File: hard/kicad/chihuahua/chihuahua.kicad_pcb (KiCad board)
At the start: 2 copper layers, 97.8 x 72.4 mm, 36 parts, among them J1 CARTRIDGE, J2 VIAport, J3 IOx, J4 nanoLink, J5 STEP, J6 POWER, Q1 BC548, Q2 BC548, SW1 RESET, SW2 NMI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

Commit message: mostly routed Chihuahua
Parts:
- JP4: value CA1L -> LATCH; footprint Connector_PinHeader_2.54mm:PinHeader_1x02_P2.54mm_Horizontal -> Connector_PinHeader_2.54mm:PinHeader_1x02_P2.54mm_Vertical
- R3, R4: value R -> 3K3
- R5: value R -> 1K
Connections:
- net /VIA_~IRQ renamed /~VREQ
- net Net-(JP3-Pad1) renamed /~VP
- SW1 pad 1: +5V -> /U_RST
- SW1 pad 2: /U_RST -> +5V
- U4 pad 10: /VIA_~CS -> /~IOC
- U4 pad 11: /ROM_~CS -> /ROM_~OE
- U4 pad 12: A15 -> /R~W
- U4 pad 13: /~IOC -> /VIA_~CS
- U4 pad 8: /ROM_~OE -> /ROM_~CS
- U4 pad 9: /R~W -> A15
- U5 pad 1: /R~W -> /CB2
- U5 pad 10: /CB2 -> PB7
- U5 pad 11: /CB2 -> /~WE
- U5 pad 12: /CB2 -> /R~W
- U5 pad 13: /CB2 -> /PHI1
- U5 pad 2: /PHI1 -> /CB2
- U5 pad 3: /~WE -> /CB2
- U5 pad 4: PB7 -> /CB2
- U5 pad 5: PB7 -> /CB2
- U5 pad 6: PB7 -> /CB2
- U5 pad 8: /CB2 -> PB7
- U5 pad 9: /CB2 -> PB7
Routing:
- net /~NMI: track 21.8 -> 127.0 mm, vias 0 -> 3
- net /~WE: track 91.4 -> 0.00 mm, vias 2 -> 0
- net +5V: track 230.8 -> 300.6 mm, vias 1 -> 4
- net /~IOC: track 0.00 -> 66.0 mm, vias 0 -> 1
- net GND: track 340.9 -> 279.3 mm
- net /CA2: track 52.4 -> 0.00 mm, vias 1 -> 0
- net /CA1: track 46.6 -> 0.00 mm, vias 1 -> 0
- net A10: track 26.6 -> 69.0 mm, vias 0 -> 1
- net A11: track 26.6 -> 66.6 mm, vias 0 -> 1
- net PB2: track 4.86 -> 40.4 mm, vias 0 -> 1
- net PB1: track 4.86 -> 39.5 mm, vias 0 -> 1
- net PB0: track 4.86 -> 38.6 mm, vias 0 -> 1
- net A9: track 26.6 -> 59.5 mm, vias 0 -> 1
- net A0: track 42.8 -> 71.3 mm, vias 0 -> 1
- net A1: track 42.8 -> 70.9 mm, vias 0 -> 1
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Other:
- net class Default: clearance 0.2 -> 0.15; trace_width 0.25 -> 0.2; via_dia 0.8 -> 0.55; via_drill 0.4 -> 0.35
- net class LowZ added: clearance 0.2, trace_width 0.635, via_dia 0.8, via_drill 0.5
- net class Power added: clearance 0.15, trace_width 0.28, via_dia 0.55, via_drill 0.35
- rule trace_clearance: 0.2 -> 0.15
- rule trace_min: 0.2 -> 0.127
- rule via_min_size: 0.4 -> 0.5

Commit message: completely routed Chihuahua
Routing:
- net /CA1: track 0.00 -> 162.0 mm, vias 0 -> 3
- net /ROM_~CS: track 0.00 -> 93.4 mm, vias 0 -> 3
- net /ROM_~OE: track 0.00 -> 84.3 mm, vias 0 -> 2
- net /~WE: track 0.00 -> 75.9 mm
- net /VIA_CS: track 0.00 -> 67.4 mm, vias 0 -> 2
- net /CA2: track 0.00 -> 66.9 mm, vias 0 -> 3
- net /PHI1: track 0.00 -> 61.8 mm, vias 0 -> 1
- net +5V: track 300.6 -> 360.6 mm, vias 4 -> 5
- net /VIA_~CS: track 0.00 -> 35.3 mm, vias 0 -> 3
- net /CB2: track 69.8 -> 104.9 mm, vias 1 -> 2
- net PB4: track 42.2 -> 74.2 mm, vias 1 -> 2
- net PB3: track 41.3 -> 72.9 mm, vias 1 -> 2
- net PB1: track 39.5 -> 70.1 mm, vias 1 -> 3
- net PB0: track 38.6 -> 68.8 mm, vias 1 -> 3
- net PB2: track 40.4 -> 69.8 mm, vias 1 -> 3
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
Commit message: finish silkscreen, not sure about /IOC
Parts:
- added LOGO1: Logo_Open_Hardware_Large, Symbol:OSHW-Symbol_8.9x8mm_SilkScreen, B.Cu at (48.3, 50.8)
- added LOGO2: Logo_Open_Hardware_Small, durango:jaqueria, B.Cu at (91.4, 20.3)
- D1: footprint Diode_THT:D_DO-35_SOD27_P2.54mm_Vertical_AnodeUp -> Diode_THT:D_DO-35_SOD27_P2.54mm_Vertical_KathodeUp
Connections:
- J1 pad 4: /~IOC -> PB5
- U4 pad 10: /~IOC -> PB5
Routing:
- net PB5: track 21.5 -> 114.3 mm, vias 0 -> 2
- net /~IOC: track 66.0 -> 0.00 mm, vias 1 -> 0
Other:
- board text added: "+"
- board text added: "+5 GND PA0 PA5 PA1 PA6 PA2 PA7 PA3 CA1 PA4 CA2 GND +5V"
- board text added: "+5 GND PB0 PB5 PB1 PB6 PB2 PB7 PB3 CB1 PB4 CB2 GND +5V"
- board text added: "+5 PD0 BA0 PD1 BA1 PD2 BA2 PD3 BA3 PD4 /WR PD5 /IO PD6 GND PD7"
- board text added: "@zuiko21"
- board text added: "Chihuahua PLUS v1 (2023·10)"
- board text added: "D"
- board text added: "GND SSCL SSDA ~STB +5"
- board text added: "JLCJLCJLCJLC"
- board text added: "K"
- board text added: "x"
- board text added: "x D C G"
- board text added: "~C"

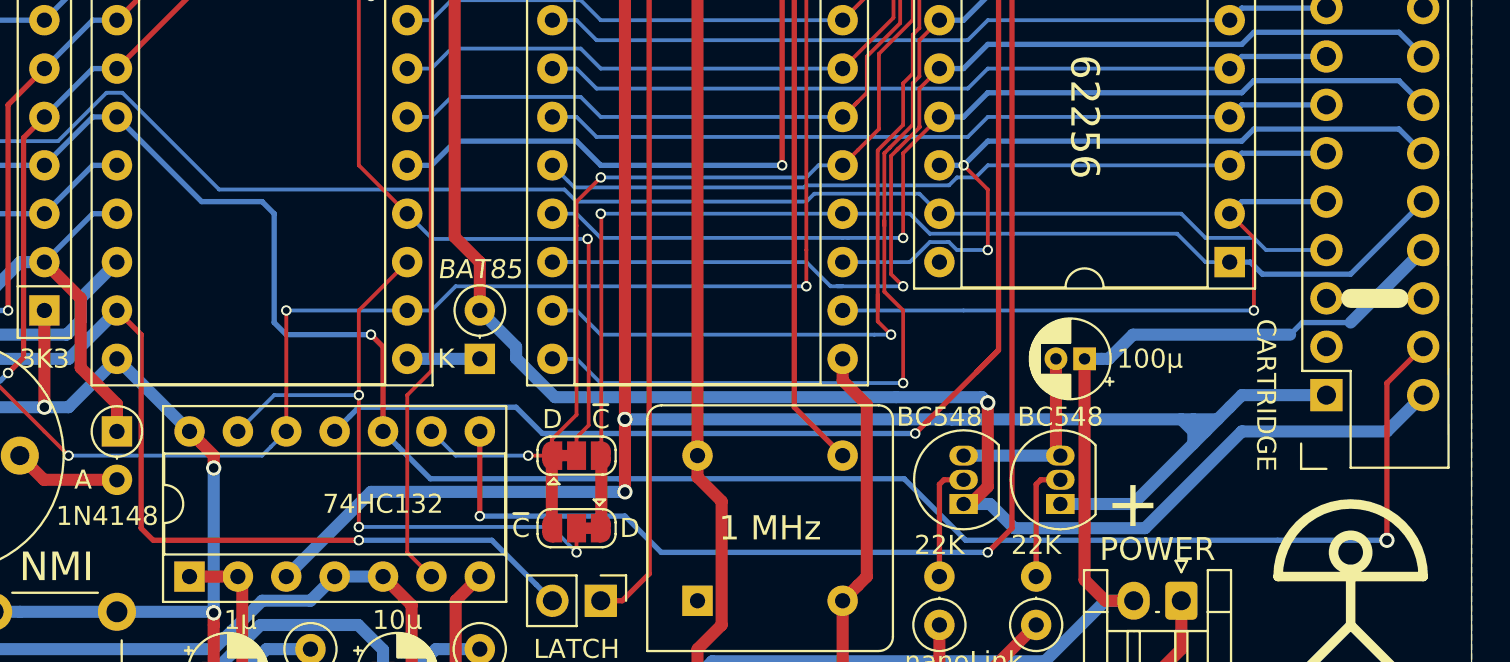
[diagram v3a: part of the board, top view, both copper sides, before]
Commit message: completely remove /IOC from Chihuahua
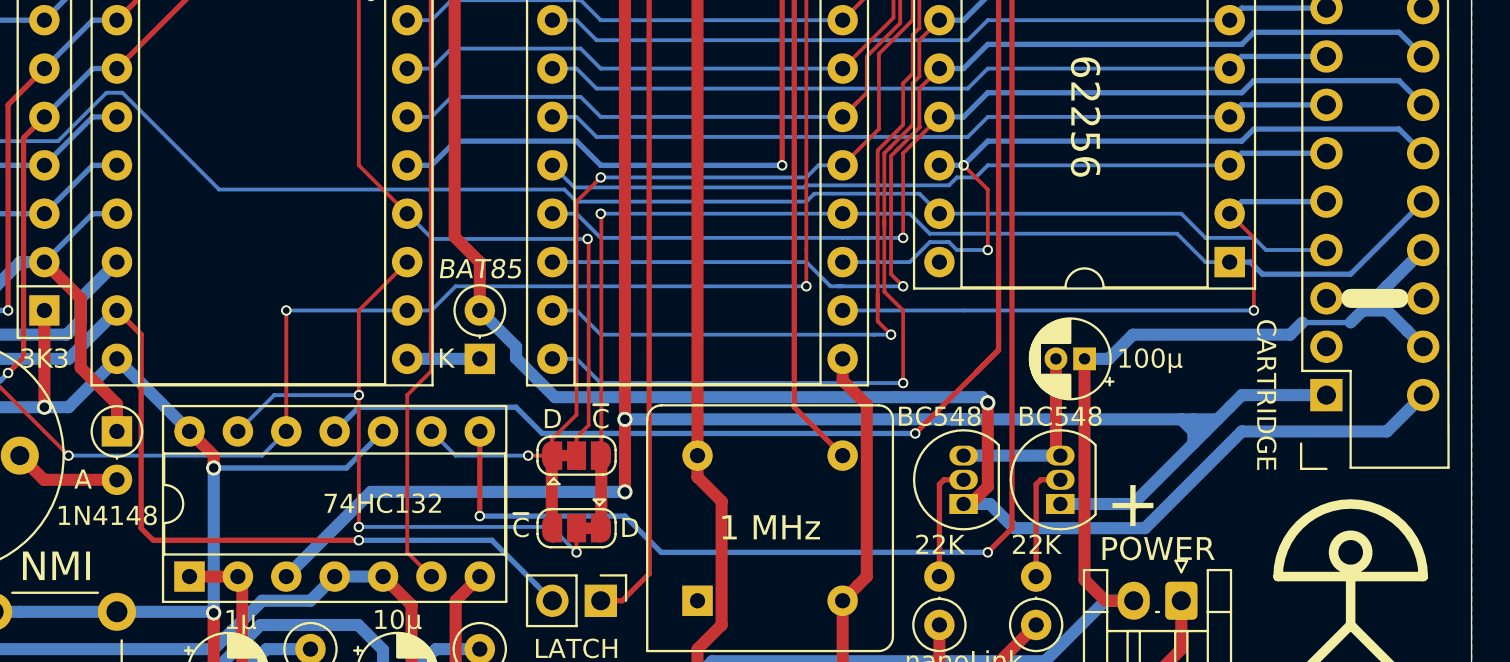
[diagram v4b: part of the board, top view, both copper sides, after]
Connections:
- J1 pad 4: PB5 -> +5V
- U4 pad 10: PB5 -> +5V
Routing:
- net PB5: track 114.3 -> 21.5 mm, vias 2 -> 0
- net +5V: track 360.6 -> 376.4 mm
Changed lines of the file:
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@@
     (thickness 1.6)
     (drawings 31)
-    (tracks 1024)
+    (tracks 1014)
     (zones 0)
     (modules 38)
@@
   )
   (setup
-    (last_trace_width 0.28)
+    (last_trace_width 0.635)
     (user_trace_width 0.2)
     (user_trace_width 0.28)
@@
       (net 68 /U_RST))
     (pad 10 thru_hole oval (at 7.62 10.16 90) (size 1.6 1.6) (drill 0.8) (layers *.Cu *.Mask)
-      (net 17 PB5))
+      (net 2 +5V))
     (pad 3 thru_hole oval (at 0 5.08 90) (size 1.6 1.6) (drill 0.8) (layers *.Cu *.Mask)
       (net 9 /~NMI))
@@
       (net 10 /~IRQ))
     (pad 4 thru_hole oval (at -1.27 5.715 180) (size 1.7 1.7) (drill 1) (layers *.Cu *.Mask)
-      (net 17 PB5))
+      (net 2 +5V))
     (pad 5 thru_hole oval (at 3.81 8.255 180) (size 1.7 1.7) (drill 1) (layers *.Cu *.Mask))
     (pad 3 thru_hole oval (at 3.81 5.715 180) (size 1.7 1.7) (drill 1) (layers *.Cu *.Mask))
@@
   (segment (start 19.111101 18.988899) (end 26.380299 18.988899) (width 0.635) (layer B.Cu) (net 2))
   (segment (start 17.78 20.32) (end 19.111101 18.988899) (width 0.635) (layer B.Cu) (net 2))
-  (segment (start 105.41 64.135) (end 109.22 60.325) (width 0.635) (layer B.Cu) (net 2))
-  (segment (start 91.44 66.04) (end 92.32 66.04) (width 0.635) (layer B.Cu) (net 2))
   (segment (start 92.535 78.74) (end 94.02 78.74) (width 0.635) (layer F.Cu) (net 2))
   (segment (start 91.44 77.645) (end 92.535 78.74) (width 0.635) (layer F.Cu) (net 2))
@@
   (segment (start 71.12 27.94) (end 78.74 27.94) (width 0.635) (layer B.Cu) (net 2))
   (segment (start 68.58 27.94) (end 71.12 27.94) (width 0.635) (layer B.Cu) (net 2))
-  (segment (start 92.32 66.04) (end 92.71 66.04) (width 0.635) (layer B.Cu) (net 2))
-  (segment (start 92.71 66.04) (end 93.98 64.77) (width 0.635) (layer B.Cu) (net 2))
-  (segment (start 93.98 64.77) (end 102.235 64.77) (width 0.635) (layer B.Cu) (net 2))
-  (segment (start 102.235 64.77) (end 102.87 64.135) (width 0.28) (layer B.Cu) (net 2))
   (segment (start 102.87 64.135) (end 105.41 64.135) (width 0.28) (layer B.Cu) (net 2))
   (segment (start 17.78 50.8) (end 19.05 49.53) (width 0.28) (layer B.Cu) (net 2))
@@
   (segment (start 32.496799 55.700001) (end 22.404999 55.700001) (width 0.28) (layer B.Cu) (net 17))
   (segment (start 22.225 55.88) (end 21.59 55.88) (width 0.28) (layer B.Cu) (net 17))
+  (segment (start 52.69 71.77) (end 54.61 69.85) (width 0.28) (layer B.Cu) (net 2))
+  (segment (start 45.72 71.77) (end 52.69 71.77) (width 0.28) (layer B.Cu) (net 2))
+  (segment (start 108.370001 64.555001) (end 109.22 65.405) (width 0.635) (layer B.Cu) (net 2))
+  (segment (start 107.315 63.5) (end 107.315 62.23) (width 0.635) (layer B.Cu) (net 2))
+  (segment (start 106.68 62.865) (end 107.315 62.23) (width 0.635) (layer B.Cu) (net 2))
+  (segment (start 107.315 62.23) (end 109.22 60.325) (width 0.635) (layer B.Cu) (net 2))
+  (segment (start 106.68 62.865) (end 107.315 63.5) (width 0.635) (layer B.Cu) (net 2))
+  (segment (start 107.315 63.5) (end 108.370001 64.555001) (width 0.635) (layer B.Cu) (net 2))
+  (segment (start 106.045 63.5) (end 107.315 63.5) (width 0.635) (layer B.Cu) (net 2))
+  (segment (start 105.41 64.135) (end 106.045 63.5) (width 0.635) (layer B.Cu) (net 2))
+  (segment (start 106.045 63.5) (end 106.68 62.865) (width 0.635) (layer B.Cu) (net 2))
+  (segment (start 102.235 64.77) (end 102.87 64.135) (width 0.635) (layer B.Cu) (net 2))
+  (segment (start 93.98 64.77) (end 102.235 64.77) (width 0.635) (layer B.Cu) (net 2))
+  (segment (start 92.71 66.04) (end 93.98 64.77) (width 0.635) (layer B.Cu) (net 2))
+  (segment (start 91.44 66.04) (end 92.71 66.04) (width 0.635) (layer B.Cu) (net 2))
   (segment (start 39.37 40.64) (end 36.83 43.18) (width 0.28) (layer B.Cu) (net 18))
   (segment (start 40.64 40.64) (end 39.37 40.64) (width 0.28) (layer B.Cu) (net 18))
@@
   (segment (start 69.215 76.2) (end 67.31 74.295) (width 0.28) (layer B.Cu) (net 31))
   (segment (start 59.69 74.295) (end 59.69 69.85) (width 0.28) (layer F.Cu) (net 31))
-  (segment (start 54.61 69.85) (end 55.409999 70.649999) (width 0.28) (layer B.Cu) (net 17))
-  (segment (start 57.094999 72.334999) (end 66.978799 72.334999) (width 0.28) (layer B.Cu) (net 17))
-  (segment (start 55.409999 70.649999) (end 57.094999 72.334999) (width 0.28) (layer B.Cu) (net 17))
-  (segment (start 81.967997 72.334999) (end 85.197998 75.565) (width 0.28) (layer B.Cu) (net 17))
-  (segment (start 66.978799 72.334999) (end 81.967997 72.334999) (width 0.28) (layer B.Cu) (net 17))
-  (via (at 107.315 75.565) (size 0.8) (drill 0.5) (layers F.Cu B.Cu) (net 17))
-  (segment (start 101.57637 75.565) (end 107.315 75.565) (width 0.28) (layer B.Cu) (net 17))
-  (segment (start 85.197998 75.565) (end 101.57637 75.565) (width 0.28) (layer B.Cu) (net 17))
-  (segment (start 107.315 67.31) (end 109.22 65.405) (width 0.28) (layer F.Cu) (net 17))
-  (segment (start 107.315 75.565) (end 107.315 67.31) (width 0.28) (layer F.Cu) (net 17))
-  (via (at 53.975 64.77) (size 0.55) (drill 0.35) (layers F.Cu B.Cu) (net 17))
-  (segment (start 54.61 65.405) (end 53.975 64.77) (width 0.28) (layer F.Cu) (net 17))
-  (segment (start 54.61 69.85) (end 54.61 65.405) (width 0.28) (layer F.Cu) (net 17))
-  (segment (start 49.53 64.77) (end 53.975 64.77) (width 0.28) (layer B.Cu) (net 17))
-  (segment (start 48.895 64.135) (end 49.53 64.77) (width 0.28) (layer B.Cu) (net 17))
-  (segment (start 48.895 58.42) (end 48.895 64.135) (width 0.28) (layer B.Cu) (net 17))
-  (segment (start 48.26 57.785) (end 48.895 58.42) (width 0.28) (layer B.Cu) (net 17))
-  (segment (start 45.085 57.785) (end 48.26 57.785) (width 0.28) (layer B.Cu) (net 17))
-  (segment (start 40.64 53.34) (end 45.085 57.785) (width 0.28) (layer B.Cu) (net 17))
   (segment (start 78.74 71.12) (end 76.2 68.58) (width 0.28) (layer F.Cu) (net 32))
   (segment (start 76.2 68.58) (end 76.2 27.94) (width 0.28) (layer F.Cu) (net 32))

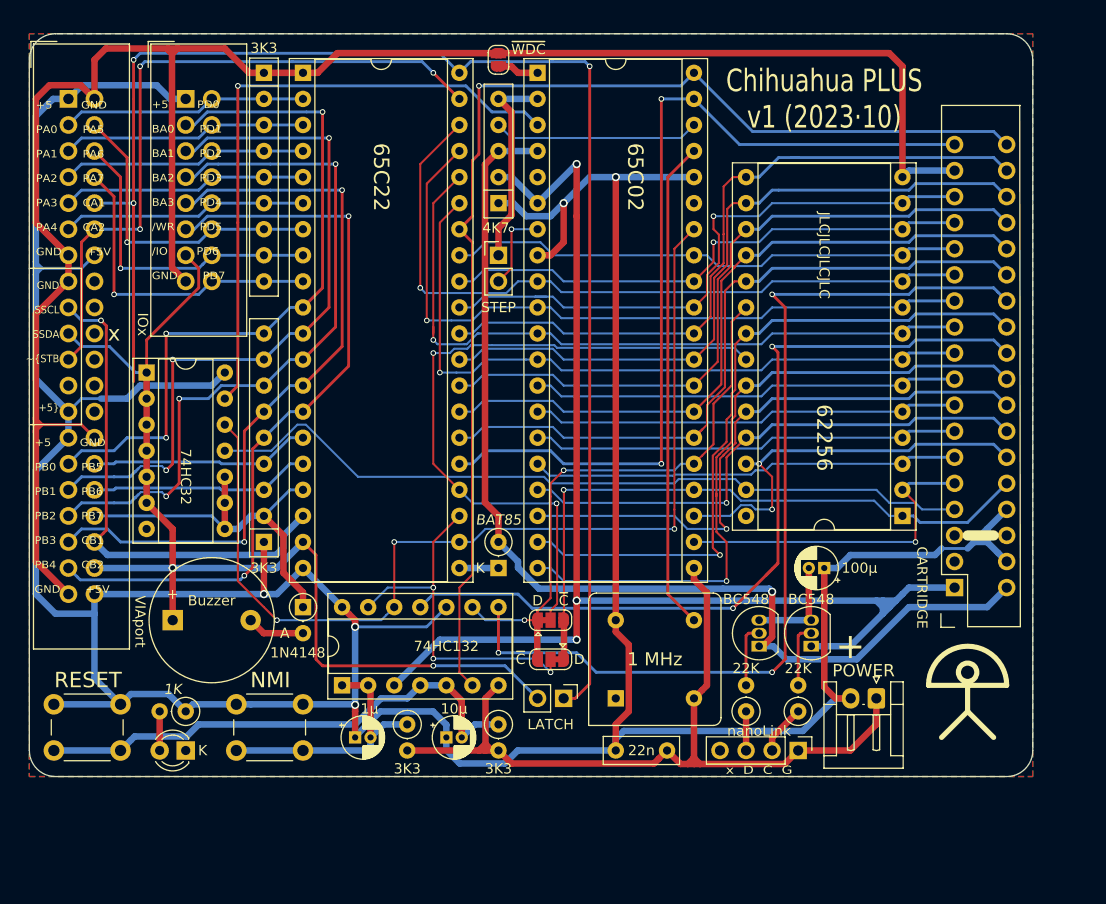
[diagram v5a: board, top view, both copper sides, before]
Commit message: add holes and thicken tracks
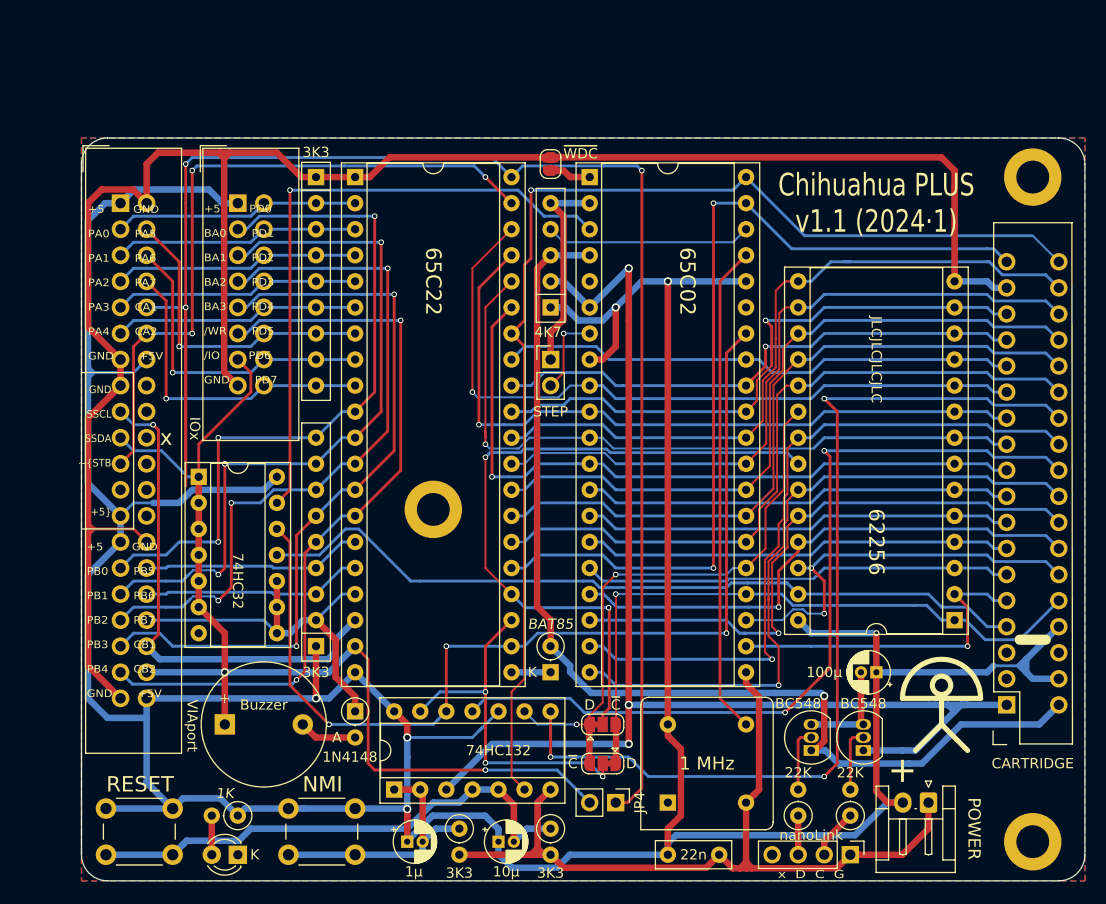
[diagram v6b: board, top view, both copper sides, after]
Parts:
- added H1: MountingHole_Pad, MountingHole:MountingHole_3.2mm_M3_DIN965_Pad, F.Cu at (111.8, 27.9)
- added H2: MountingHole_Pad, MountingHole:MountingHole_3.2mm_M3_DIN965_Pad, F.Cu at (111.8, 92.7)
- added H3: MountingHole_Pad, MountingHole:MountingHole_3.2mm_M3_DIN965_Pad, F.Cu at (53.3, 60.3)
- moved LOGO1 18.5 mm to (53.3, 68.6)
- moved J1 12.5 mm to (113.0, 82.5)
- moved SW1 11.4 mm to (27.9, 94.0)
- moved C4 11.4 mm to (76.2, 94.0)
- moved D2 11.4 mm to (45.7, 80.0)
- moved D3 11.4 mm to (34.3, 94.0)
- moved J4 11.4 mm to (94.0, 94.0)
- moved J6 11.4 mm to (101.6, 88.9)
- moved JP4 11.4 mm to (71.1, 88.9)
- moved SW2 11.4 mm to (45.7, 94.0)
- moved X1 11.4 mm to (76.2, 88.9)
- moved U3 11.4 mm to (104.1, 71.1)
- moved R2 11.4 mm to (88.9, 90.2)
- moved BZ1 11.4 mm to (33.0, 81.3)
- moved R4 11.4 mm to (55.9, 91.4)
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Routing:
- net +5V: track 376.4 -> 388.0 mm, vias 5 -> 6
- net /~WE: track 75.9 -> 85.1 mm
- net D3: track 69.2 -> 69.9 mm
- net A14: track 62.6 -> 63.3 mm
- net D2: track 59.2 -> 58.7 mm
- net /~IRQ: track 105.6 -> 105.1 mm
- net /SCLK: track 86.7 -> 87.2 mm
- net /~RST: track 115.6 -> 116.2 mm
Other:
- outline, holes or cut-outs redrawn
- board text added: "Chihuahua PLUS v1.1 (2024·1)"
- board text removed: "Chihuahua PLUS v1 (2023·10)"
